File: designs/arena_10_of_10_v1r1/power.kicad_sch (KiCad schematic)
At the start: 4 parts, among them J25 Barrel_Jack, J26 Barrel_Jack, SW1 SW_SPDT, U82 RB-XXYYD

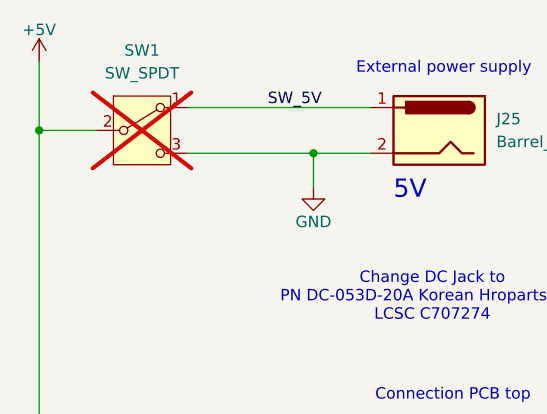
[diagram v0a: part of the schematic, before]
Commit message: Tightened DRC rules, increased via sizes, and added switch
Added power switch SW1.

Assemble pin sockets for Teensy (J100/J101, 1x24 pin sockets; J102, 2x3 pin socket, 2mm pitch for ethernet).

Tightened board-setup DRC limits to match JLCPCB 6-layer minimums:

- min_hole_to_hole 0.25 -> 0.5 mm,
- min_text_thickness 0.08 -> 0.15 mm,
- min_via_annular_width 0.05 -> 0.075 mm.

Set stackup copper_finish from "None" to "ENIG".

Added PCB title block and automatic name / revision / date on silkscreen.

Refreshed footprints from library (0402/1210/SOT-23 crtyd now  uses fp_rect).

produced v1.1.2.
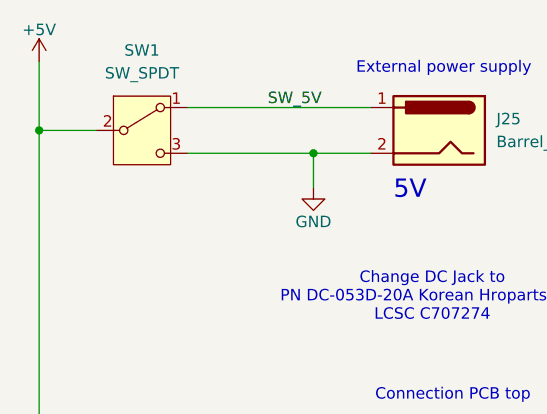
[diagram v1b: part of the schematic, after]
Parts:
- SW1: LCSC Part # (none) -> C19189125; now fitted; now in the parts list
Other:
- company: (none) -> IORodeo for Reiser Lab @ Janelia | HHMI
- title: (none) -> G6 Teensy 10-10 Arena
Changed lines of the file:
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@@
 	(generator_version "9.0")
 	(paper "A4")
+	(title_block
+		(title "G6 Teensy 10-10 Arena")
+		(date "2026-04-22")
+		(rev "v1.1.2")
+		(company "IORodeo for Reiser Lab @ Janelia | HHMI")
+	)
 	(text "Change DC Jack to\nPN DC-053D-20A Korean Hroparts Elec \nLCSC C707274\n"
 		(exclude_from_sim no)
@@
 		)
 		(instances
-			(project ""
+			(project "arena_10_of_10_v1r1"
 				(path "/056666d2-2c8f-491c-bcad-db3c517779a8/f8e525f6-92ff-481c-b9d6-983b91f2917d"
 					(reference "#PWR0284")
@@
 		)
 		(instances
-			(project ""
+			(project "arena_10_of_10_v1r1"
 				(path "/056666d2-2c8f-491c-bcad-db3c517779a8/f8e525f6-92ff-481c-b9d6-983b91f2917d"
 					(reference "#PWR0248")
@@
 		)
 		(instances
-			(project ""
+			(project "arena_10_of_10_v1r1"
 				(path "/056666d2-2c8f-491c-bcad-db3c517779a8/f8e525f6-92ff-481c-b9d6-983b91f2917d"
 					(reference "J25")
@@
 		)
 		(instances
-			(project ""
+			(project "arena_10_of_10_v1r1"
 				(path "/056666d2-2c8f-491c-bcad-db3c517779a8/f8e525f6-92ff-481c-b9d6-983b91f2917d"
 					(reference "#PWR0250")
@@
 		)
 		(instances
-			(project ""
+			(project "arena_10_of_10_v1r1"
 				(path "/056666d2-2c8f-491c-bcad-db3c517779a8/f8e525f6-92ff-481c-b9d6-983b91f2917d"
 					(reference "#PWR0285")
@@
 		)
 		(instances
-			(project ""
+			(project "arena_10_of_10_v1r1"
 				(path "/056666d2-2c8f-491c-bcad-db3c517779a8/f8e525f6-92ff-481c-b9d6-983b91f2917d"
 					(reference "#PWR0286")
@@
 		)
 		(instances
-			(project ""
+			(project "arena_10_of_10_v1r1"
 				(path "/056666d2-2c8f-491c-bcad-db3c517779a8/f8e525f6-92ff-481c-b9d6-983b91f2917d"
 					(reference "U82")
@@
 		(unit 1)
 		(exclude_from_sim no)
-		(in_bom no)
-		(on_board yes)
-		(dnp yes)
+		(in_bom yes)
+		(on_board yes)
+		(dnp no)
 		(fields_autoplaced yes)
 		(property "Reference" "SW1"
@@
 			)
 		)
+		(property "LCSC Part #" "C19189125"
+			(at 44.45 31.75 0)
+			(effects
+				(font
+					(size 1.27 1.27)
+				)
+				(hide yes)
+			)
+		)
 		(pin "2"
 		)
@@
 		)
 		(instances
-			(project ""
+			(project "arena_10_of_10_v1r1"
 				(path "/056666d2-2c8f-491c-bcad-db3c517779a8/f8e525f6-92ff-481c-b9d6-983b91f2917d"
 					(reference "SW1")
